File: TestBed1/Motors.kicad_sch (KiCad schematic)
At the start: 6 parts, among them J1 X27Motor, J3 X27Motor, J4 X27Motor

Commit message: WIP Adding new sheets.
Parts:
- removed D1, D2, D3: D, symbol Device:D

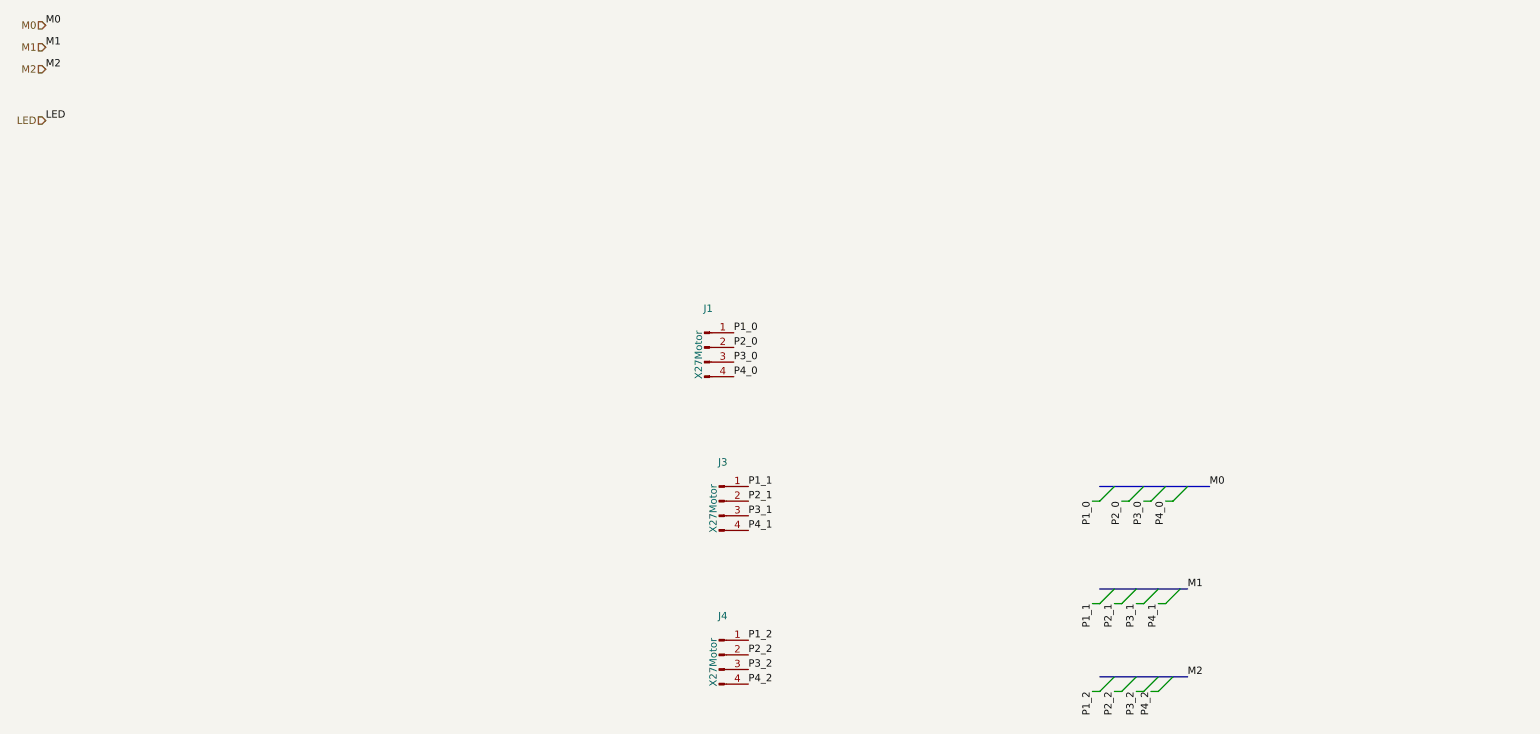
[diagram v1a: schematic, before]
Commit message: Schematic Assignment, board assignemtn and rough placement
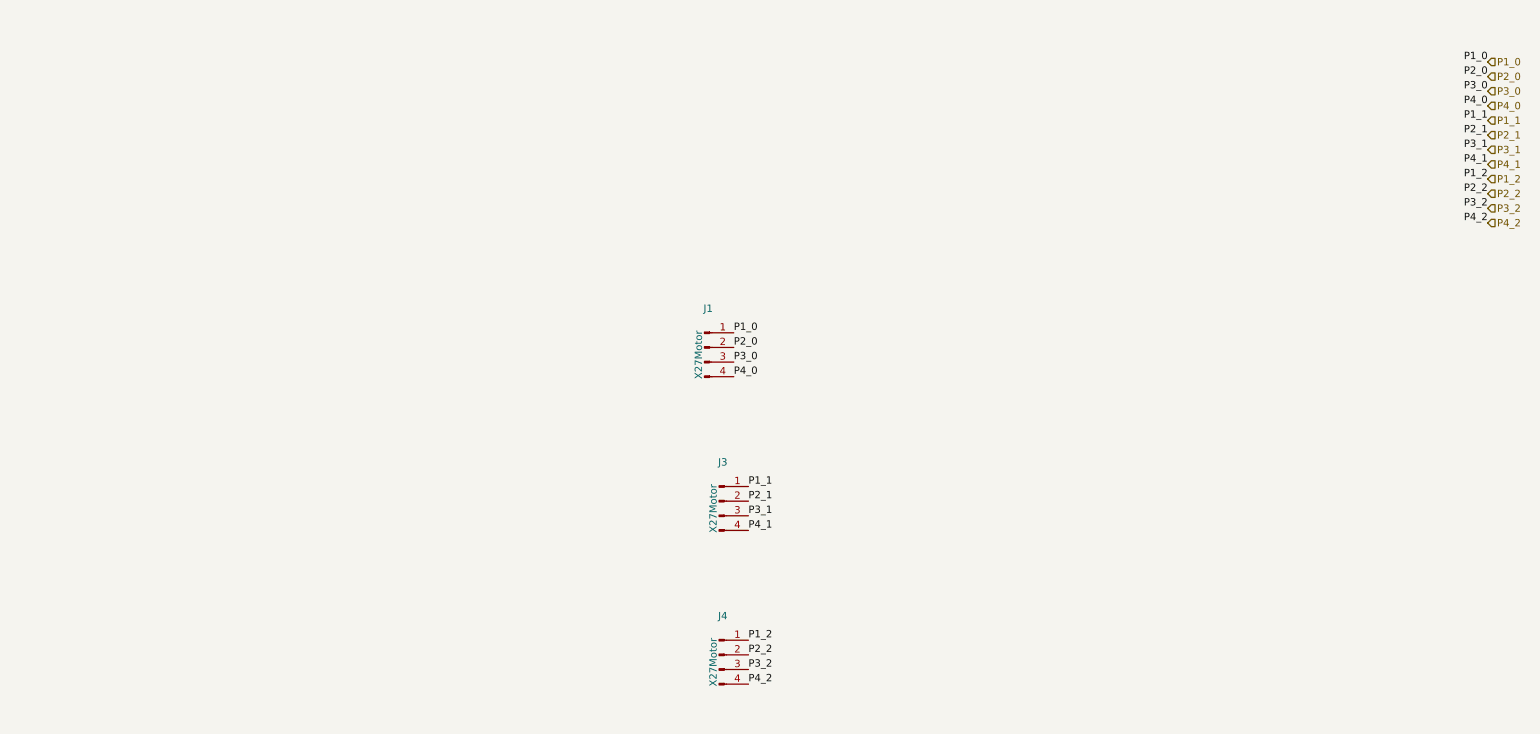
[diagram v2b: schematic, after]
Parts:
- J1, J3, J4: footprint Library:X27-168 -> X27:X27-168
